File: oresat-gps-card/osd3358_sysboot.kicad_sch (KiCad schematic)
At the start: 28 parts, among them J5 Conn_01x06, U1 OSD3358-512M-BSM

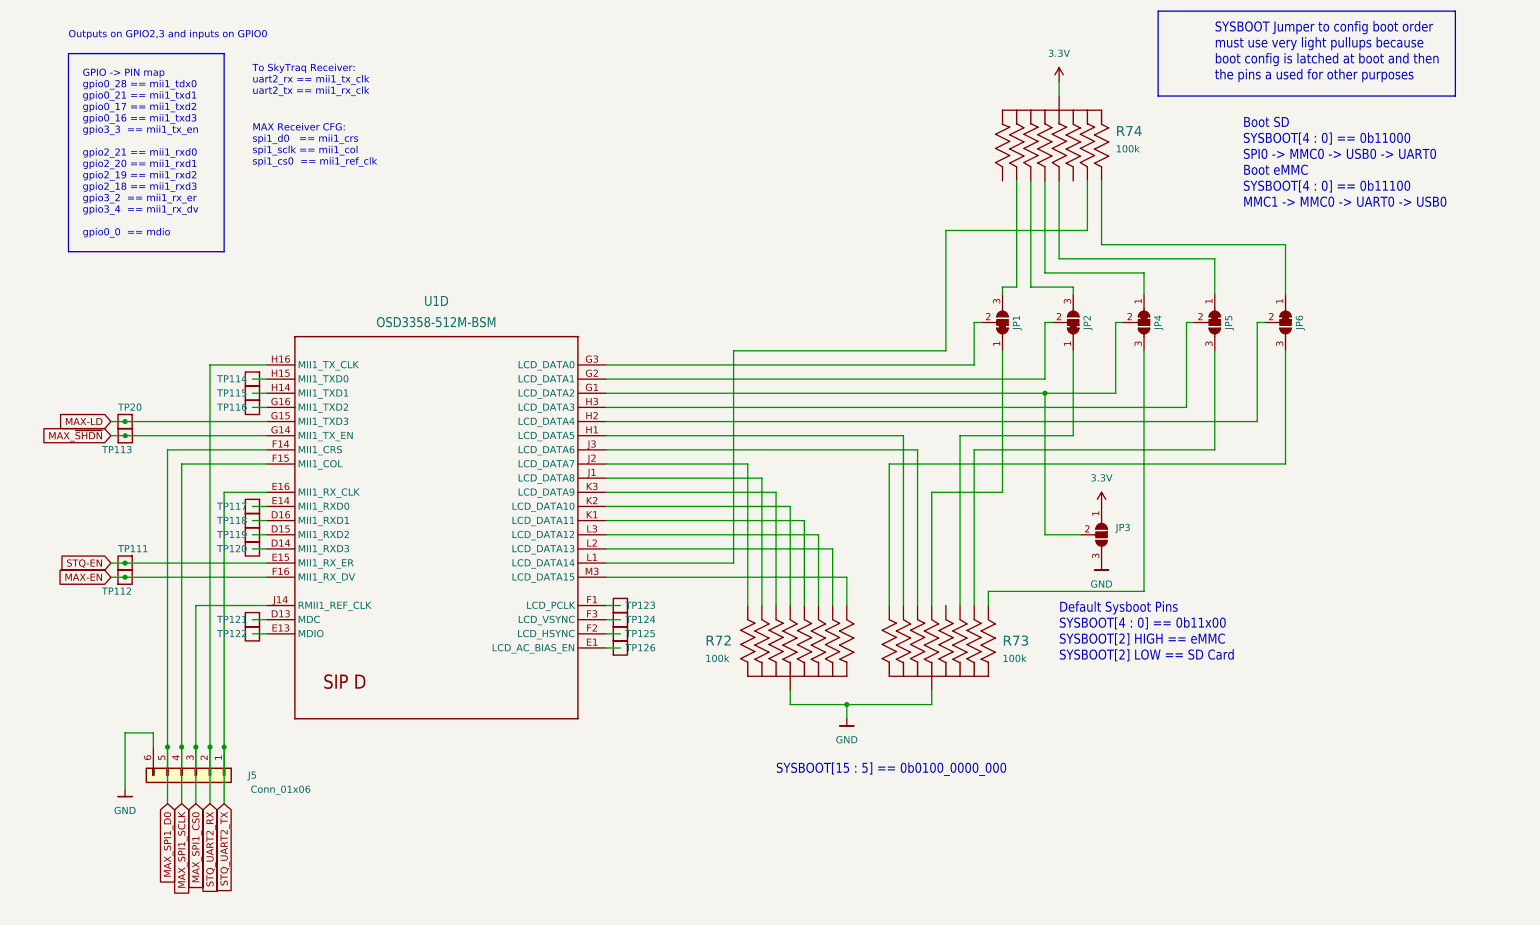
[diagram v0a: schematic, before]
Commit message: GPS card design review changes and issue fixes
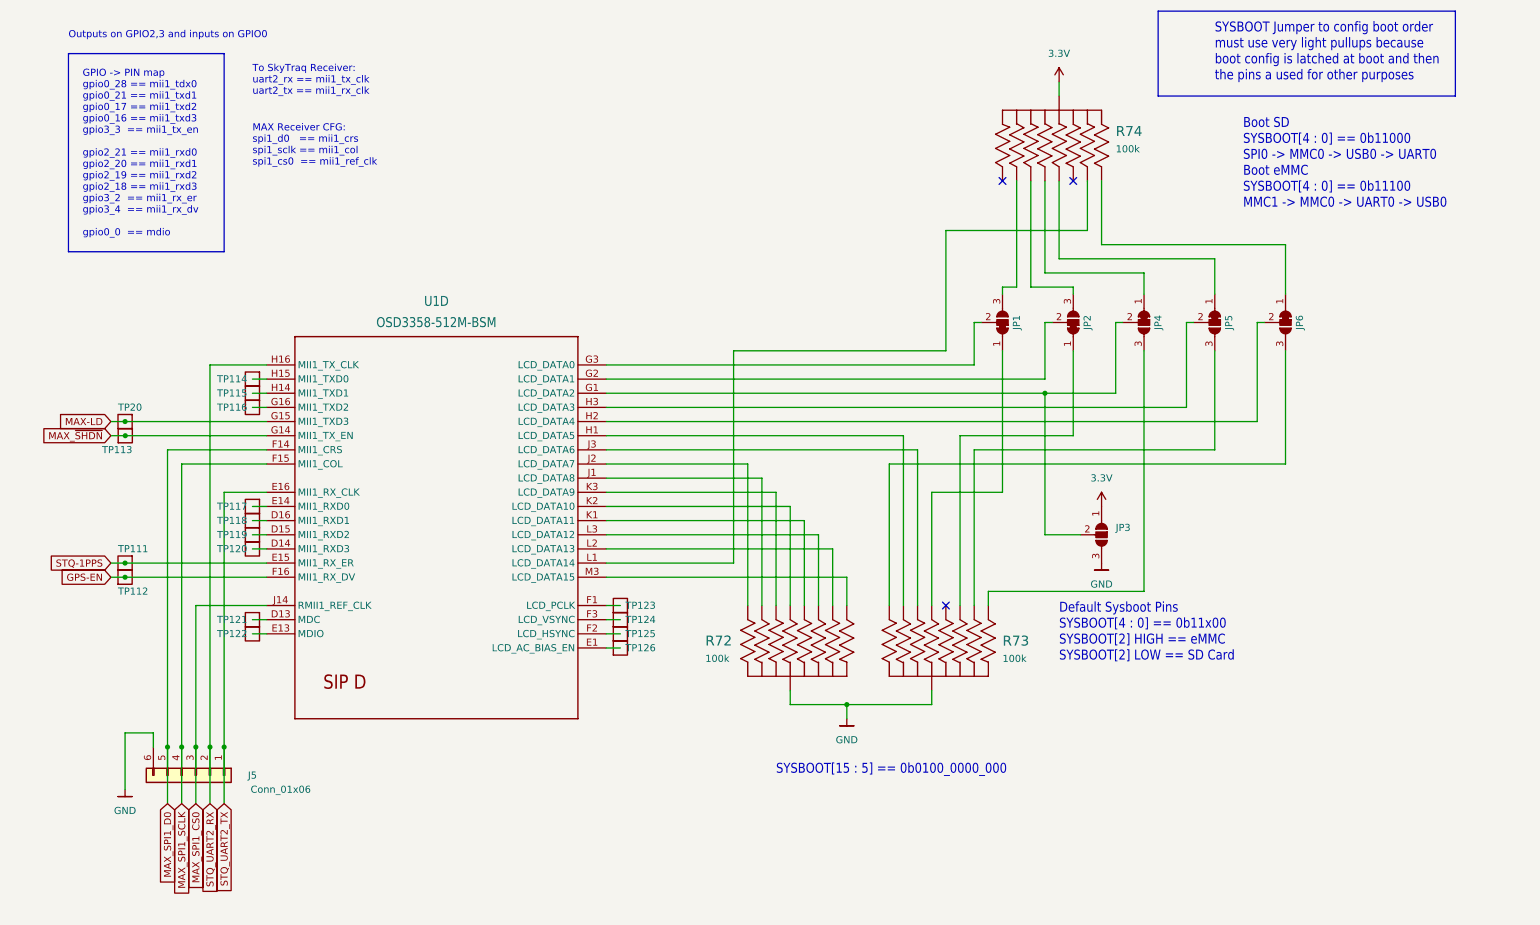
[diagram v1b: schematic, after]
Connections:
- net MAX-EN renamed GPS-EN
- net STQ-EN renamed STQ-1PPS
- no-connect marks 0 -> 3
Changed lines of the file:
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@@
   (junction (at 53.34 154.94) (diameter 0) (color 0 0 0 0)
   )
+  (junction (at 50.8 154.94) (diameter 0) (color 0 0 0 0)
+  )
   (junction (at 35.56 124.46) (diameter 0) (color 0 0 0 0)
   )
-  (junction (at 50.8 154.94) (diameter 0) (color 0 0 0 0)
-  )
   (junction (at 35.56 121.92) (diameter 0) (color 0 0 0 0)
   )
@@
   (junction (at 165.1 147.32) (diameter 0) (color 0 0 0 0)
   )
+  (no_connect (at 193.04 53.34))
+  (no_connect (at 205.74 53.34))
+  (no_connect (at 182.88 129.54))
   (wire (pts (xy 208.28 53.34) (xy 208.28 62.23))
     (stroke (width 0) (type default) (color 0 0 0 0))
@@
     (stroke (width 0) (type default) (color 0 0 0 0))
   )
+  (wire (pts (xy 33.02 124.46) (xy 35.56 124.46))
+    (stroke (width 0) (type default) (color 0 0 0 0))
+  )
   (wire (pts (xy 121.92 91.44) (xy 200.66 91.44))
     (stroke (width 0) (type default) (color 0 0 0 0))
@@
     (stroke (width 0) (type default) (color 0 0 0 0))
   )
-  (wire (pts (xy 33.02 124.46) (xy 35.56 124.46))
-    (stroke (width 0) (type default) (color 0 0 0 0))
-  )
   (wire (pts (xy 121.92 96.52) (xy 238.76 96.52))
     (stroke (width 0) (type default) (color 0 0 0 0))
@@
     (stroke (width 0) (type default) (color 0 0 0 0))
   )
+  (wire (pts (xy 35.56 124.46) (xy 60.96 124.46))
+    (stroke (width 0) (type default) (color 0 0 0 0))
+  )
   (wire (pts (xy 205.74 72.39) (xy 198.12 72.39))
     (stroke (width 0) (type default) (color 0 0 0 0))
@@
   )
   (wire (pts (xy 200.66 78.74) (xy 201.93 78.74))
-    (stroke (width 0) (type default) (color 0 0 0 0))
-  )
-  (wire (pts (xy 35.56 124.46) (xy 60.96 124.46))
     (stroke (width 0) (type default) (color 0 0 0 0))
   )
@@
     (effects (font (size 1.27 1.27)) (justify left bottom))
   )
-  (global_label "STQ-EN" (shape input) (at 33.02 121.92 180) (fields_autoplaced)
+  (global_label "GPS-EN" (shape input) (at 33.02 124.46 180) (fields_autoplaced)
     (effects (font (size 1.27 1.27)) (justify right))
-    (property "Intersheet References" "${INTERSHEET_REFS}" (id 0) (at 23.0474 121.8406 0)
+    (property "Intersheet References" "${INTERSHEET_REFS}" (id 0) (at 22.8055 124.3806 0)
       (effects (font (size 1.27 1.27)) (justify right) hide)
     )
@@
     )
   )
+  (global_label "STQ-1PPS" (shape input) (at 33.02 121.92 180) (fields_autoplaced)
+    (effects (font (size 1.27 1.27)) (justify right))
+    (property "Intersheet References" "${INTERSHEET_REFS}" (id 0) (at 20.5679 121.8406 0)
+      (effects (font (size 1.27 1.27)) (justify right) hide)
+    )
+  )
   (global_label "MAX_SPI1_CS0" (shape input) (at 48.26 165.1 270) (fields_autoplaced)
     (effects (font (size 1.27 1.27)) (justify right))
     (property "Intersheet References" "${INTERSHEET_REFS}" (id 0) (at 48.1806 181.1807 90)
-      (effects (font (size 1.27 1.27)) (justify right) hide)
-    )
-  )
-  (global_label "MAX-EN" (shape input) (at 33.02 124.46 180) (fields_autoplaced)
-    (effects (font (size 1.27 1.27)) (justify right))
-    (property "Intersheet References" "${INTERSHEET_REFS}" (id 0) (at 22.8055 124.3806 0)
       (effects (font (size 1.27 1.27)) (justify right) hide)
     )
@@
   (symbol (lib_id "OreSat-TestPoint:Test-Point") (at 35.56 124.46 90) (unit 1)
     (in_bom yes) (on_board yes)
-    (property "Reference" "TP112" (id 0) (at 36.83 127 90)
-      (effects (font (size 1.27 1.27)) (justify left))
+    (property "Reference" "TP112" (id 0) (at 34.29 127 90)
+      (effects (font (size 1.27 1.27)) (justify right))
     )
     (property "Value" "Test-Point" (id 1) (at 33.02 124.46 0)
